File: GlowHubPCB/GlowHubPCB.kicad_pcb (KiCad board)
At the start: 2 copper layers, 42.4 x 61.3 mm, 34 parts, among them Q2 MMBT2222A, Q3 MMBT2222A, SW1 TS-1185EC-C-D-B, SW2 TS-1185EC-C-D-B, U2 ESP32-WROOM-32E (4MB), U5 CP2102-GMR, U6 BL1117-33CX

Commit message: added qr code to pcb
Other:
- board text added: "PCB files: https://bit.ly/3poWjq4"
- board text removed: "PCB files: https://bit.ly/....."

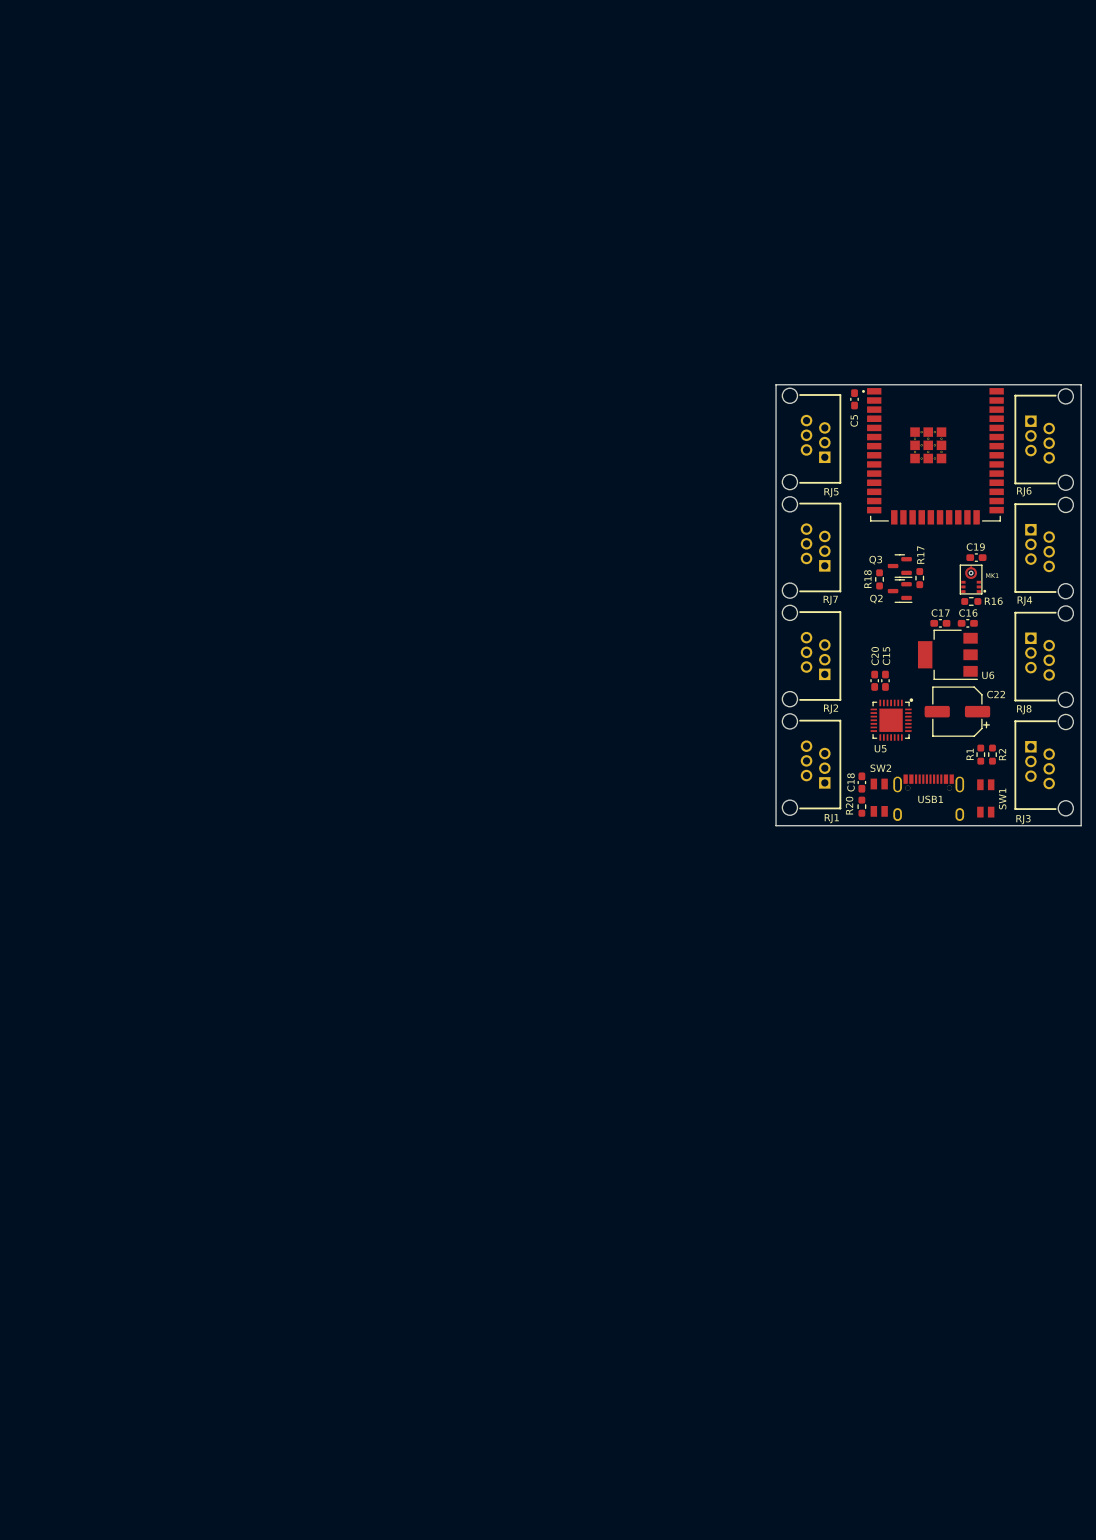
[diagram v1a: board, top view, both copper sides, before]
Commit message: added GlowHub PCB prototype
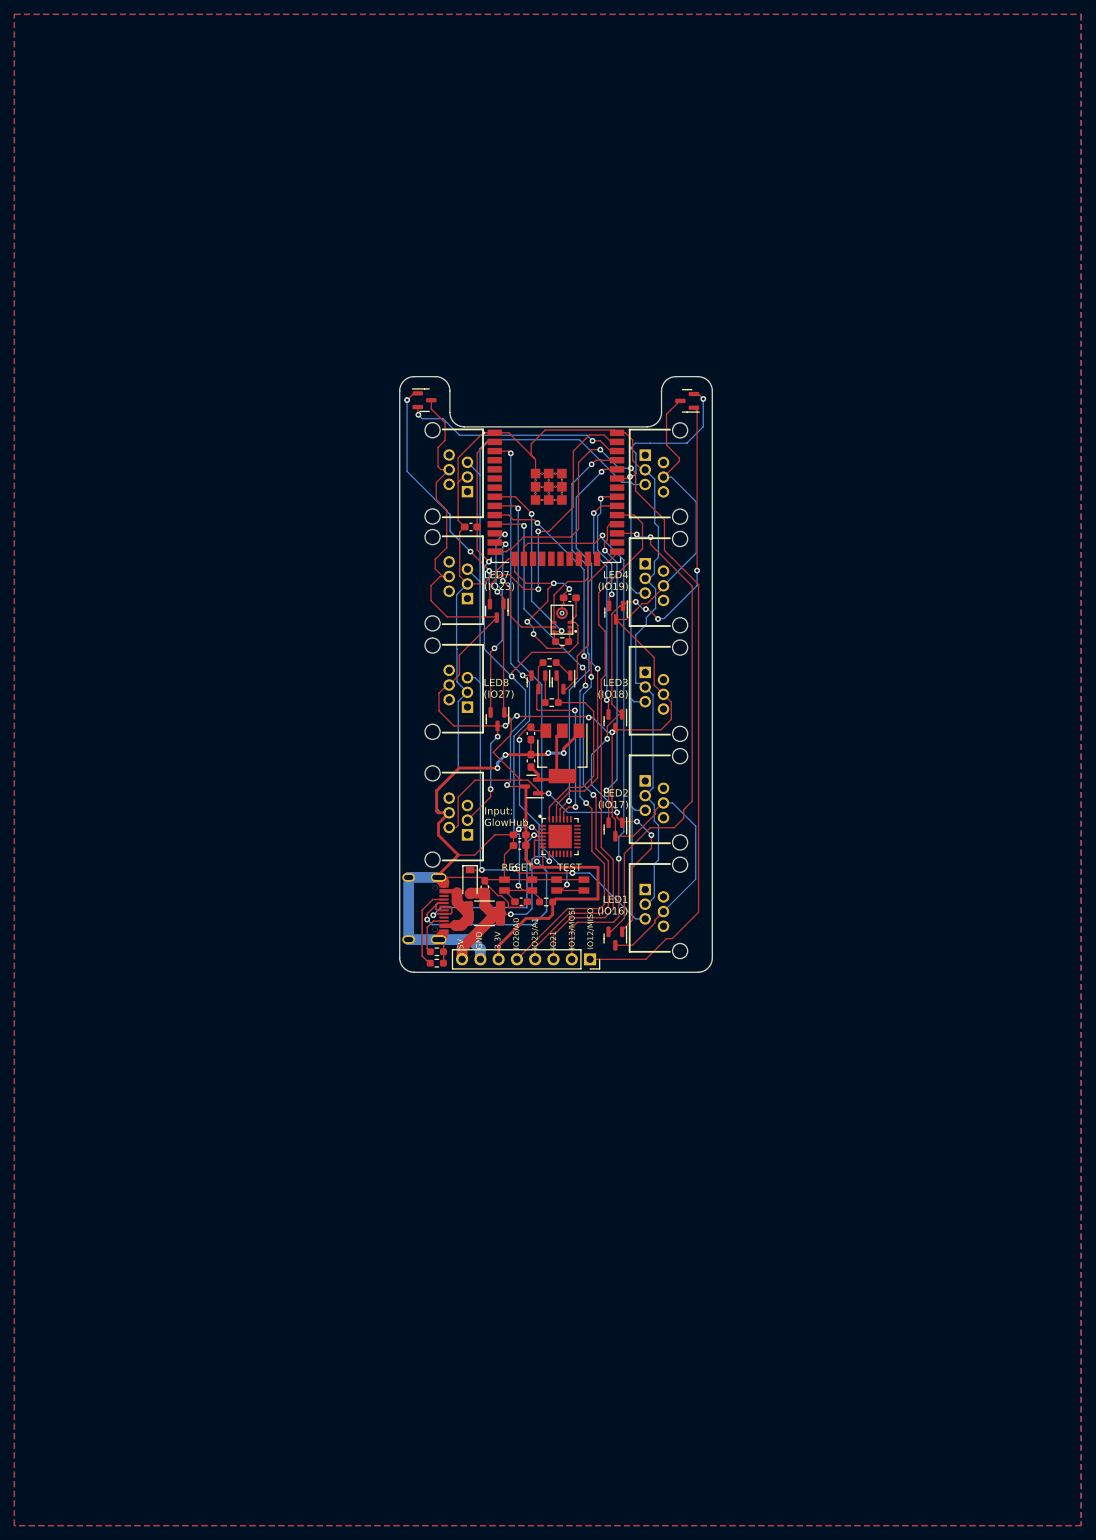
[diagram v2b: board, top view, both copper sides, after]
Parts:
- removed C22: 220uF 10V, Capacitor_SMD:CP_Elec_6.3x5.4
- added C1: 10uF, Capacitor_SMD:C_0603_1608Metric_Pad1.08x0.95mm_HandSolder, F.Cu at (64.9, 121.4)
- added D9: Schottky, Diode_SMD:D_SOD-123, F.Cu at (62.8, 120.7)
- added F1: BSMD1812-300-16V, Fuse:Fuse_1812_4532Metric_Pad1.30x3.40mm_HandSolder, F.Cu at (64.8, 125.0)
- added J1: Conn_01x08, Connector_PinSocket_2.54mm:PinSocket_1x08_P2.54mm_Vertical, F.Cu at (79.5, 131.4)
- added Q1: AP40P05, Package_TO_SOT_SMD:SOT-23, F.Cu at (83.0, 98.3)
- added Q10: AP40P05, Package_TO_SOT_SMD:SOT-23, F.Cu at (93.0, 53.8)
- added Q11: AP40P05, Package_TO_SOT_SMD:SOT-23, F.Cu at (66.6, 98.1)
- added Q4: AP40P05, Package_TO_SOT_SMD:SOT-23, F.Cu at (56.5, 53.7)
- added Q5: AP40P05, Package_TO_SOT_SMD:SOT-23, F.Cu at (71.3, 107.4)
- added Q6: AP40P05, Package_TO_SOT_SMD:SOT-23, F.Cu at (83.0, 128.5)
- added Q7: AP40P05, Package_TO_SOT_SMD:SOT-23, F.Cu at (83.1, 83.3)
- added Q8: AP40P05, Package_TO_SOT_SMD:SOT-23, F.Cu at (66.5, 83.0)
- added Q9: AP40P05, Package_TO_SOT_SMD:SOT-23, F.Cu at (83.0, 113.4)
- added RJ9: R-RJ11R06P-A800, R-RJ11R06P-A800:R-RJ11R06P-A800, F.Cu at (58.1, 111.6)
- RJ1, RJ2, RJ3, RJ4, RJ5, RJ6, RJ7, RJ8: value PCB-6P6C-90 -> R-RJ11R06P-A800
- moved RJ6 87.1 mm to (58.1, 63.9), turned to -90 degrees
- moved RJ8 87.1 mm to (58.1, 93.8), turned to -90 degrees
- moved R2 81.9 mm to (58.2, 130.4), turned to 180 degrees
- moved R1 80.9 mm to (58.2, 131.9), turned to 180 degrees
- moved USB1 71.5 mm to (56.7, 124.4), turned to -90 degrees
- moved C16 62.6 mm to (71.3, 100.0), turned to 90 degrees
- moved C17 60.0 mm to (71.3, 103.8), turned to -90 degrees
- moved SW1 59.0 mm to (76.7, 121.1), turned to 0 degrees
- moved R16 57.1 mm to (75.6, 87.3)
- moved MK1 57.1 mm to (75.6, 84.2)
- moved C19 56.8 mm to (76.7, 81.2)
- moved C5 56.2 mm to (62.9, 71.3), turned to 180 degrees
- moved U6 55.3 mm to (75.6, 102.8), turned to -90 degrees
- moved C15 55.1 mm to (69.7, 114.1), turned to 0 degrees
- moved RJ3 54.6 mm to (91.5, 94.1)
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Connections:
- net IO33/BUTTON renamed IO33/TESTBUTTON
- C17 pad 2: +3V3 -> Net-(C17-Pad2)
- RJ1 pad 4: IO16/LED1 -> LED1 DATA OUT
- RJ1 pad 5: +5V -> EXTERNAL 5V
- RJ2 pad 4: IO18/LED3 -> LED1 DATA OUT
- RJ2 pad 5: +5V -> EXTERNAL 5V
- RJ3 pad 4: IO21/LED5 -> LED1 DATA OUT
- RJ3 pad 5: +5V -> EXTERNAL 5V
- RJ4 pad 4: IO23/LED7 -> LED1 DATA OUT
- RJ4 pad 5: +5V -> EXTERNAL 5V
- RJ5 pad 4: IO17/LED2 -> LED1 DATA OUT
- RJ5 pad 5: +5V -> EXTERNAL 5V
- RJ6 pad 4: IO19/LED4 -> LED1 DATA OUT
- RJ6 pad 5: +5V -> EXTERNAL 5V
- RJ7 pad 4: IO22/LED6 -> LED1 DATA OUT
- RJ7 pad 5: +5V -> EXTERNAL 5V
- RJ8 pad 4: IO27/LED8 -> LED1 DATA OUT
- RJ8 pad 5: +5V -> EXTERNAL 5V
- U6 pad 2: +3V3 -> Net-(C17-Pad2)
- U6 pad 4: +3V3 -> Net-(C17-Pad2)
- USB1 pad A4B9: +5V -> Net-(USB1-PadA4B9)
- USB1 pad B4A9: +5V -> Net-(USB1-PadA4B9)
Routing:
- net GND: track 0.00 -> 346.9 mm, vias 0 -> 10
- net LED1 DATA OUT: track 0.00 -> 222.5 mm, vias 0 -> 6
- net RECEIVER 5V: track 0.00 -> 187.5 mm, vias 0 -> 13
- net EXTERNAL 5V: track 0.00 -> 186.2 mm, vias 0 -> 3
- net +3V3: track 0.00 -> 123.7 mm, vias 0 -> 3
- net IO12/MISO: track 0.00 -> 114.7 mm, vias 0 -> 2
- net IO13/MOSI: track 0.00 -> 79.2 mm, vias 0 -> 2
- net IO25/A1/DAC1: track 0.00 -> 78.8 mm, vias 0 -> 4
- net IO26/A0/DAC2: track 0.00 -> 77.3 mm, vias 0 -> 4
- net RESET: track 0.00 -> 76.4 mm, vias 0 -> 3
- net IO5: track 0.00 -> 74.6 mm
- net IO16/LED1: track 0.00 -> 69.0 mm, vias 0 -> 2
- net IO33/TESTBUTTON: track 0.00 -> 64.0 mm, vias 0 -> 2
- net TXD0: track 0.00 -> 56.9 mm, vias 0 -> 2
- net RXD0: track 0.00 -> 56.8 mm, vias 0 -> 2
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- added copper zone on B.Cu, net GND
- added copper zone on F.Cu, net GND
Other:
- board size 42.4 x 61.3 mm -> 43.4 x 82.8 mm
- board text added: "5V GND 3.3V IO26/A0 IO25/A1 IO21 IO13/MOSI IO12/MISO"
- board text added: "Input: 5V"
- board text added: "Input: GlowHub"
- board text added: "LED1 (IO16)"
- board text added: "LED2 (IO17)"
- board text added: "LED3 (IO18)"
- board text added: "LED4 (IO19)"
- board text added: "LED5 (IO21)"
- board text added: "LED6 (IO22)"
- board text added: "LED7 (IO23)"
- board text added: "LED8 (IO27)"
- board text added: "RESET"
- board text added: "TEST"
- board text added: "v1.0 beta 1"
- board text removed: "v0.1"

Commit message: added redesigned case
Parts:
- SW1, SW2: value TS-1185EC-C-D-B -> SW-SMD_4P-L3.7-W3.0-P1.50-LS4.7
- U5: value CP2102-GMR -> Val**
